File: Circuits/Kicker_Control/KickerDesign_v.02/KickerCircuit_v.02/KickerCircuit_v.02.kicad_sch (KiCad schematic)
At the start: 2 parts, among them P1 66200621124, P2 66200621124

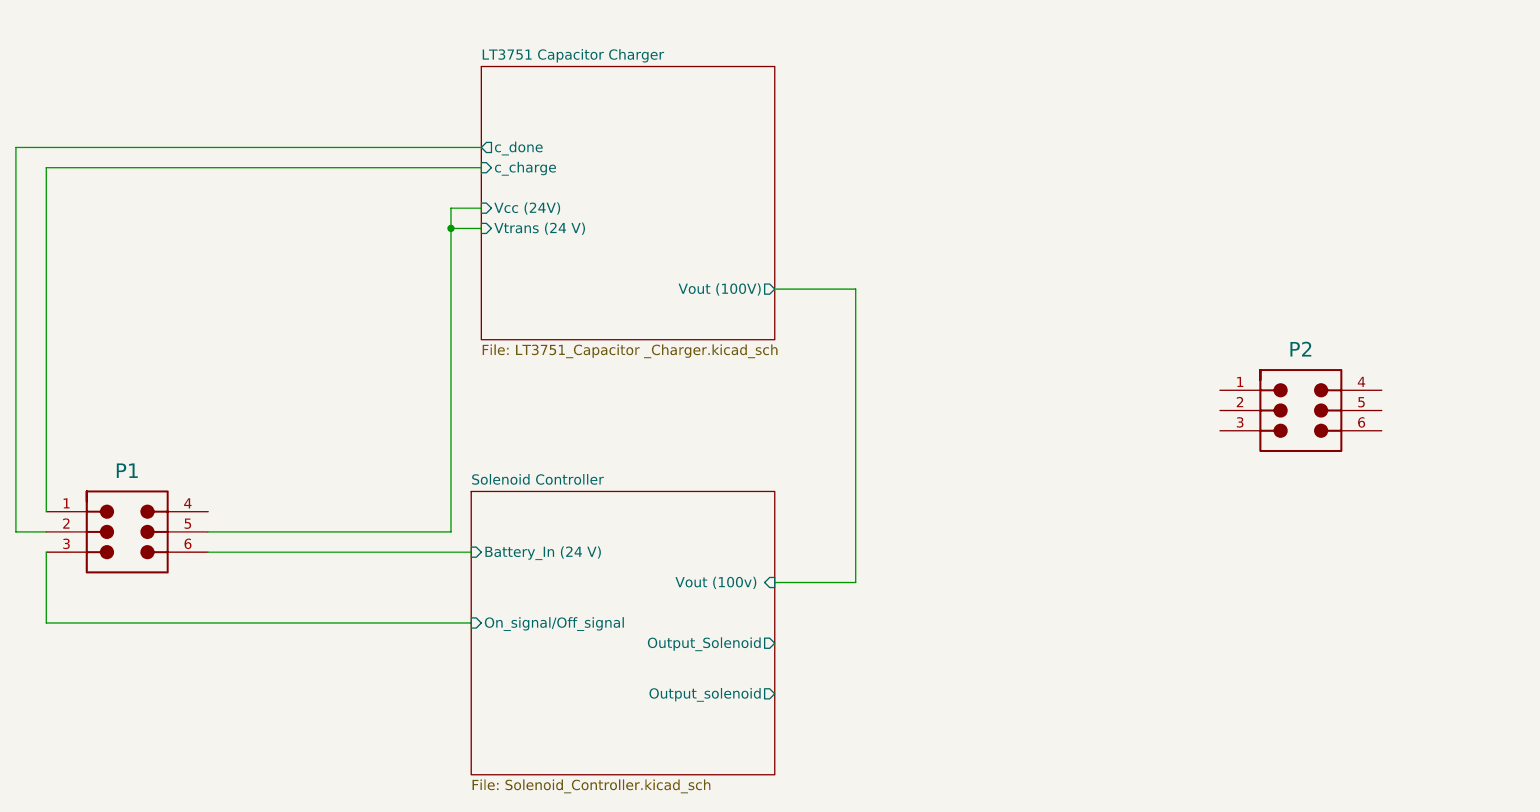
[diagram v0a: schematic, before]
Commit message: Updated the kicker circuit
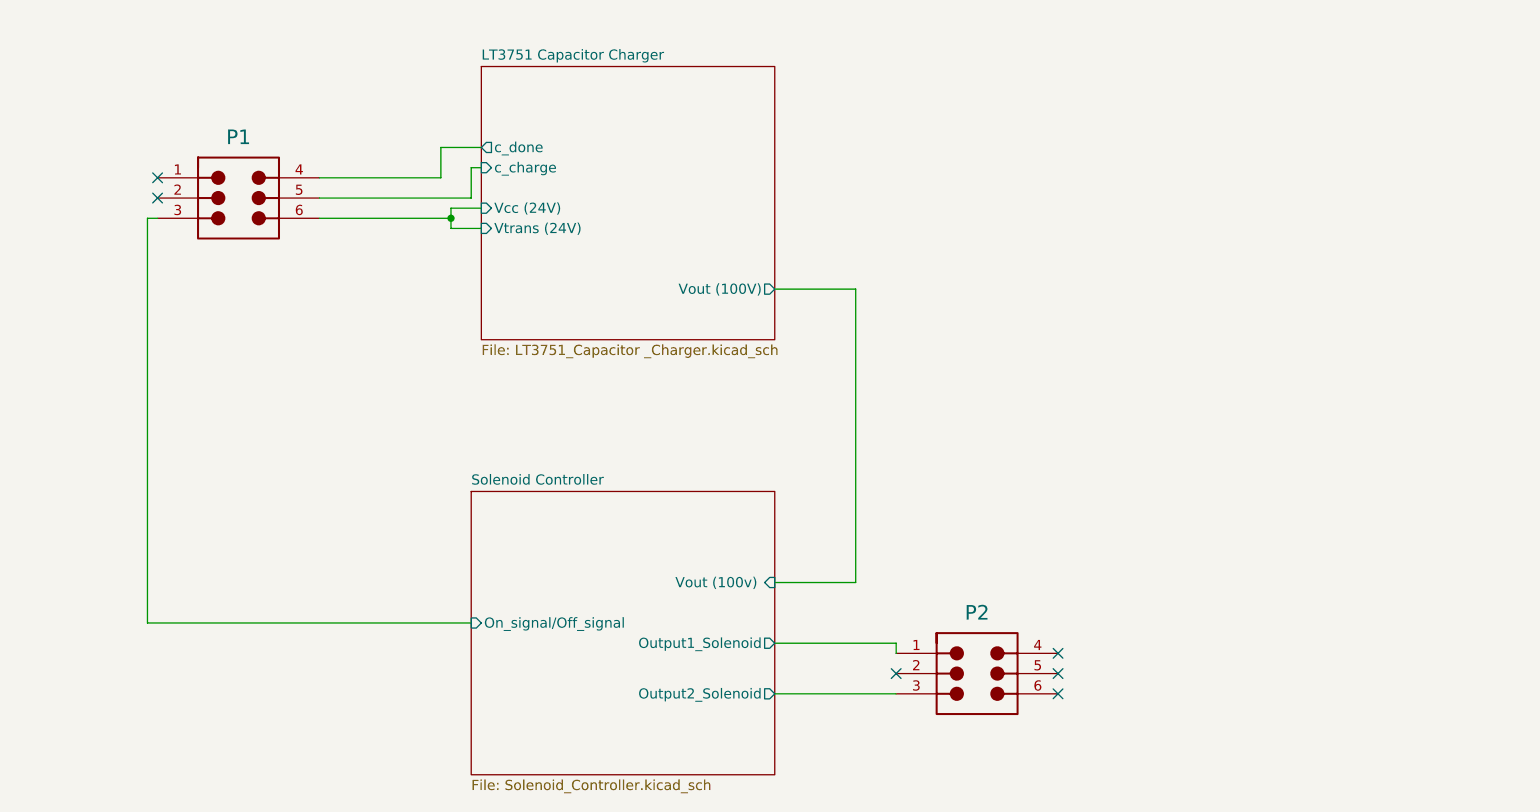
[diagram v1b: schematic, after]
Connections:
- net LT3751 Capacitor Charger/Vcc (24V) is gone; now on net LT3751 Capacitor Charger/c_charge: P1.5
- net LT3751 Capacitor Charger/c_charge: no longer P1.1
- net LT3751 Capacitor Charger/c_done: now also P1.4; no longer P1.2
- net Solenoid Controller/Output1_Solenoid: now reaches P2.1
- net Solenoid Controller/Output2_Solenoid: now reaches P2.3
- net Solenoid Controller/Battery_In (24 V)  renamed LT3751 Capacitor Charger/Vcc (24V) 
- no-connect marks 0 -> 6
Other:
- sheet LT3751 Capacitor Charger ports: added Vcc (24V) , Vtrans (24V) ; removed Vcc (24V), Vtrans (24 V) 
- sheet Solenoid Controller ports: added Output1_Solenoid, Output2_Solenoid; removed Battery_In (24 V) , Output_Solenoid, Output_solenoid
- moved on the sheet: P1, P2

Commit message: updated kicker circuit
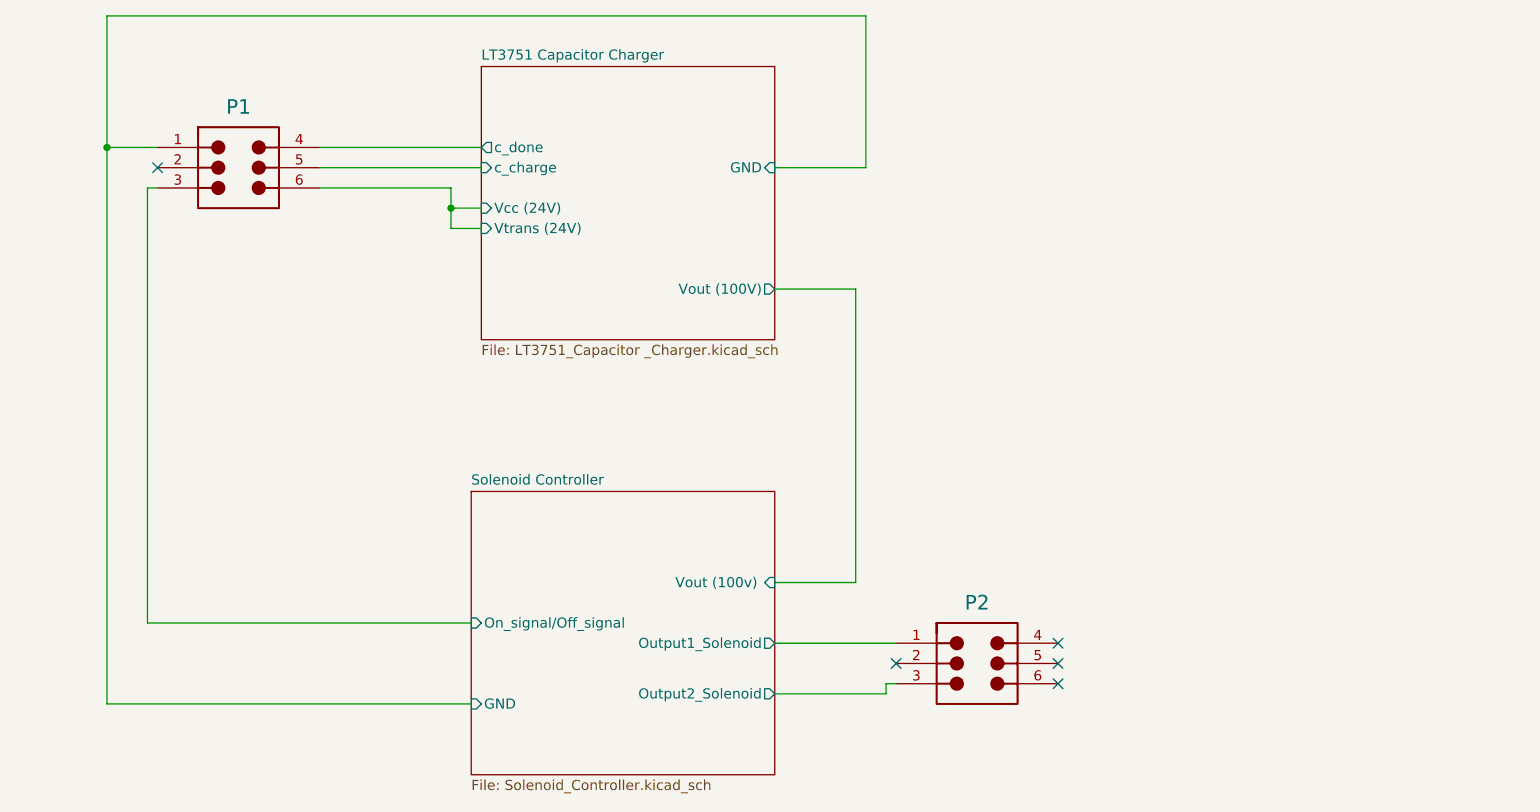
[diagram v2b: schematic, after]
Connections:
- net LT3751 Capacitor Charger/GND: now reaches P1.1
- no-connect marks 6 -> 5
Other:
- sheet LT3751 Capacitor Charger ports: added GND; removed none
- sheet Solenoid Controller ports: added GND; removed none
- moved on the sheet: P1, P2

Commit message: Changes in the circuit
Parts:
- removed P2: 66200621124, Altium_WR-MPC3 (rev23a):66200621124, symbol WR-MPC3 3.00 mm Male Header Dual Row Vertical - THT:66200621124
- added J1: Conn_01x02_Pin, symbol Connector:Conn_01x02_Pin
- added J2: Conn_01x03_Pin, Connector_PinHeader_2.54mm:PinHeader_1x03_P2.54mm_Vertical, symbol Connector:Conn_01x03_Pin
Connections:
- net Solenoid Controller/On_signal/Off_signal: now also P1.2; no longer P1.3
- net Solenoid Controller/Output1_Solenoid: now also J1.1 (Pin_1), J1.2 (Pin_2)
- new net Solenoid Controller/GND_digital: P1.3
- new net Vout(100V): J2.2 (Pin_2), J2.3 (Pin_3)
- no-connect marks 5 -> 0
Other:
- sheet Solenoid Controller ports: added GND_digital; removed GND

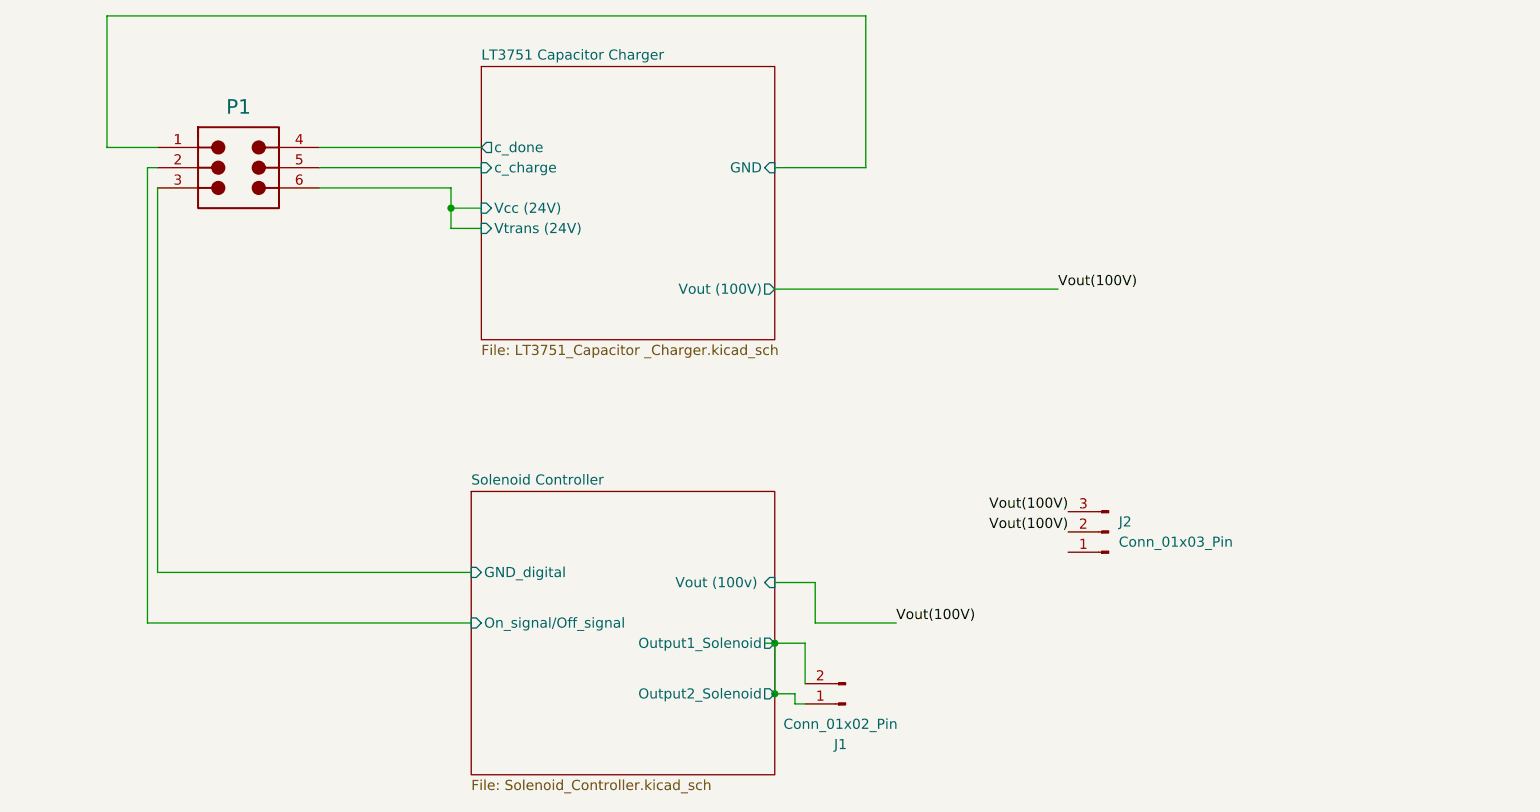
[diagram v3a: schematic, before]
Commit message: Changes in the kicker circuit
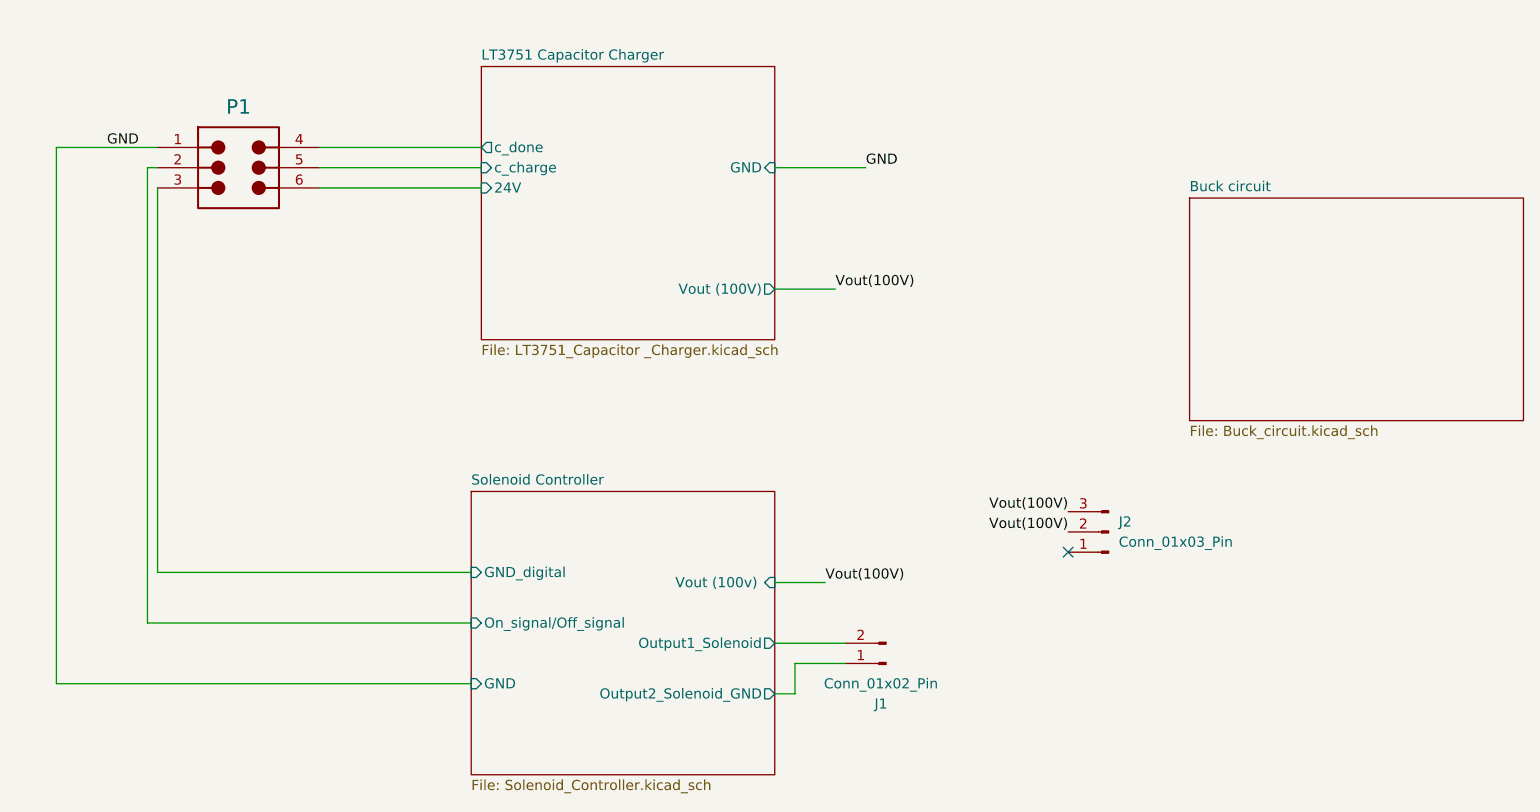
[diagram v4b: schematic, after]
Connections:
- net Solenoid Controller/Output1_Solenoid: no longer J1.1 (Pin_1)
- net LT3751 Capacitor Charger/GND renamed GND
- net LT3751 Capacitor Charger/Vcc (24V)  renamed LT3751 Capacitor Charger/24V
- new net Solenoid Controller/Output2_Solenoid_GND: J1.1 (Pin_1)
- no-connect marks 0 -> 1
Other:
- added sheet Buck circuit (Buck_circuit.kicad_sch)
- sheet LT3751 Capacitor Charger ports: added 24V; removed Vcc (24V) , Vtrans (24V) 
- sheet Solenoid Controller ports: added GND, Output2_Solenoid_GND; removed Output2_Solenoid
- moved on the sheet: J1
